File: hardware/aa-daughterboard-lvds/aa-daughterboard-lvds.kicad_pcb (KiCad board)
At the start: 4 copper layers, 148 parts, among them CN1 Barrel_Jack, CN10 6P6C, CN11 6P6C, CN12 6P6C, CN13 6P6C, CN14 Conn_01x08, CN15 Conn_01x08, CN16 Conn_01x08, CN17 8P8C, CN18 8P8C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

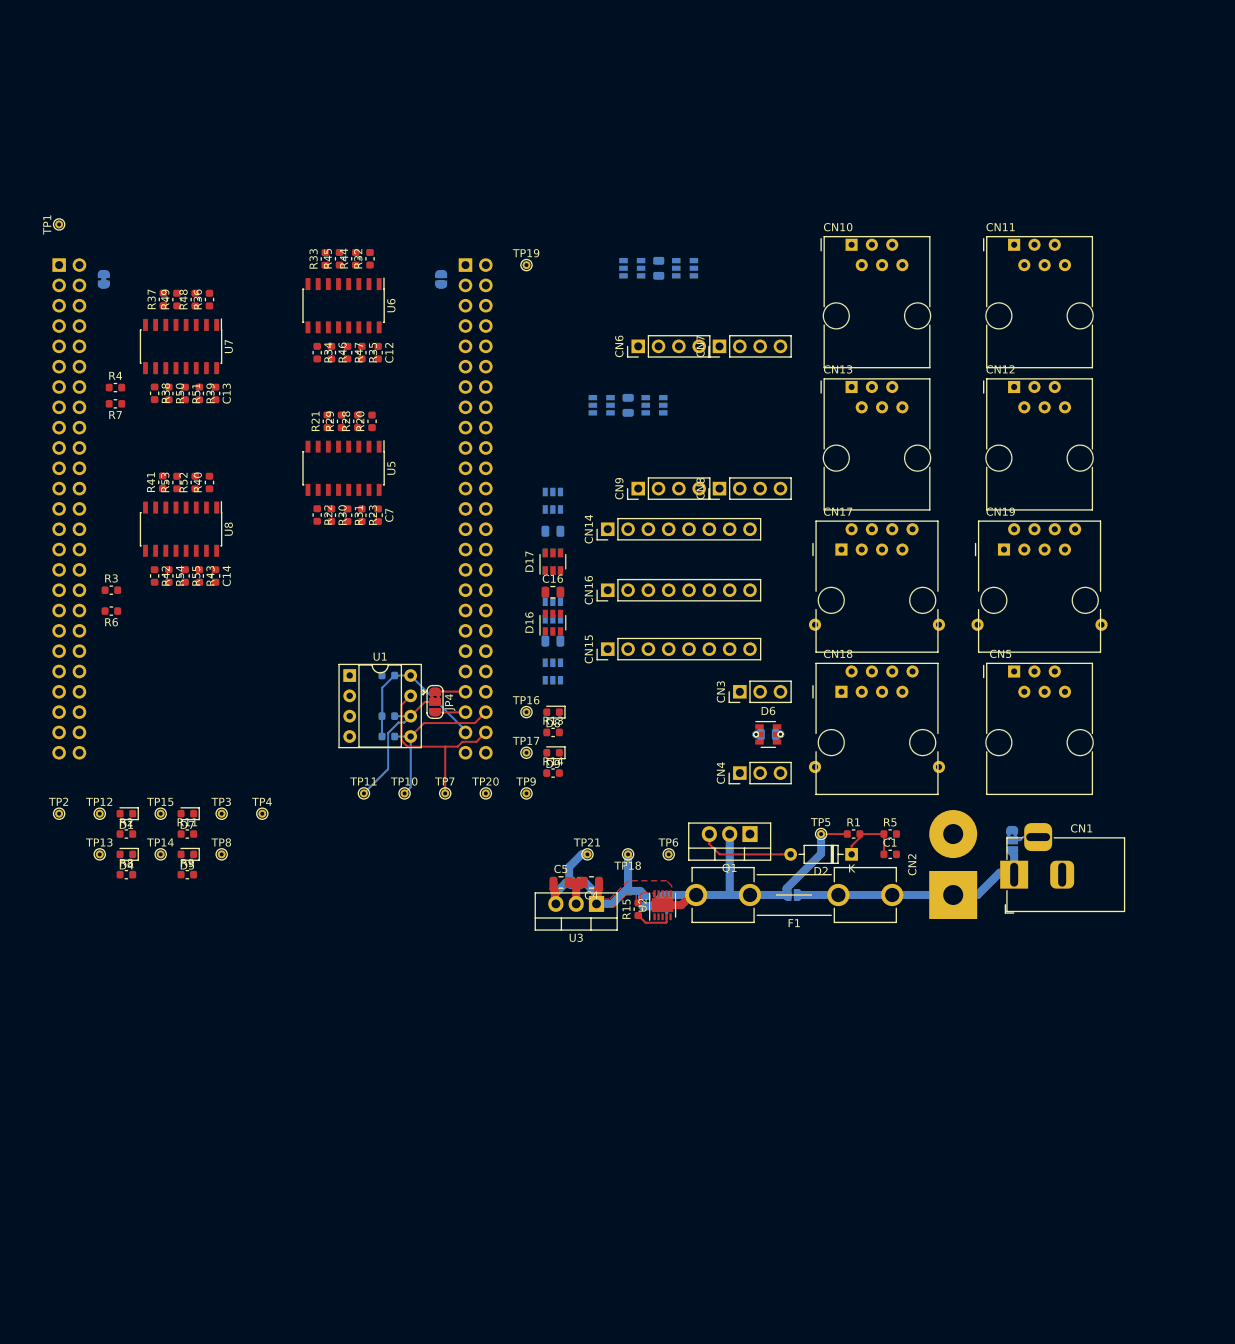
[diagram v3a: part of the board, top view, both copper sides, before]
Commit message: Name differential pairs, convert inconvenient 1x8 connectors to 2x4
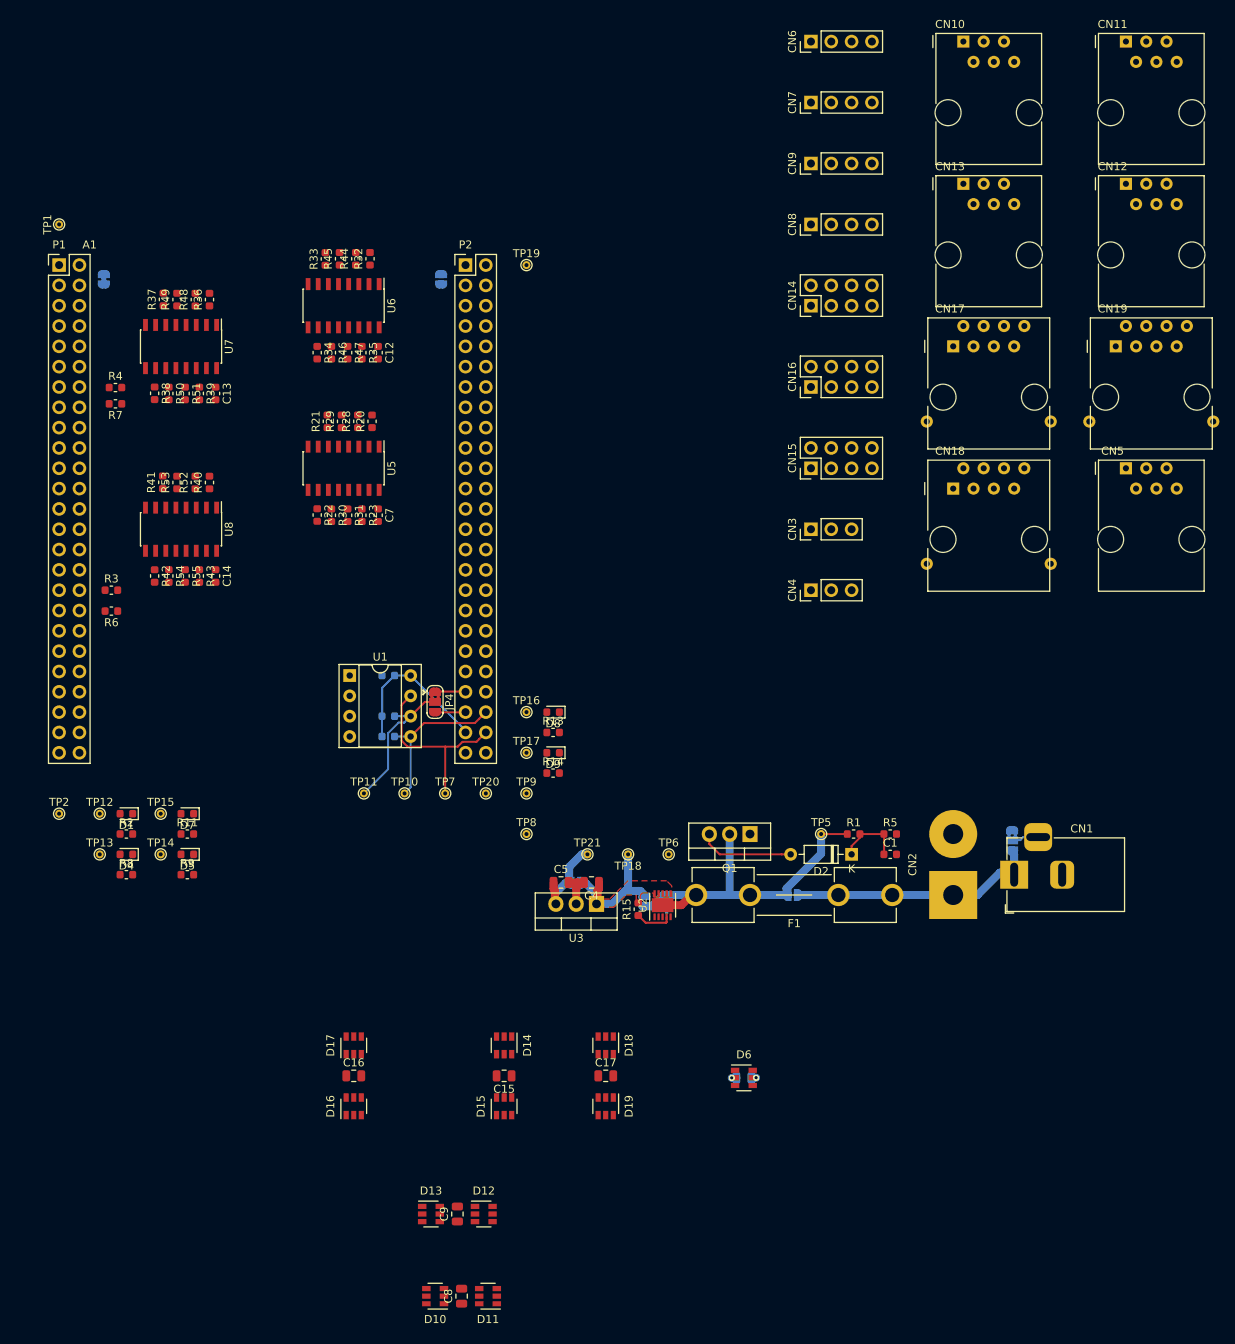
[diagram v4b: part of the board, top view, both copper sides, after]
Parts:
- removed P1, P2: Conn_02x25_Odd_Even, Connector_PinSocket_2.54mm:PinSocket_2x25_P2.54mm_Vertical
- removed TP3, TP4: TestPoint, TestPoint:TestPoint_THTPad_D1.0mm_Drill0.5mm
- added A1: STM32F407_Discovery_P1_P2, aa-daughterboard-lvds:STM32F407_Discovery_P1_P2_Socket, F.Cu at (45.7, 61.0)
- C15, C17, C8, C9, D10, D11, D12, D13, D14, D15, D18, D19: moved to F.Cu
- CN14, CN15, CN16: footprint Connector_PinHeader_2.54mm:PinHeader_1x08_P2.54mm_Vertical -> Connector_PinHeader_2.54mm:PinHeader_2x04_P2.54mm_Vertical
- moved C8 130.8 mm to (96.0, 189.8), turned to 90 degrees
- moved D10 130.8 mm to (92.7, 189.8)
- moved D11 130.8 mm to (99.3, 189.8)
- moved C9 103.3 mm to (95.5, 179.6), turned to 90 degrees
- moved D12 103.3 mm to (98.8, 179.6)
- moved D13 103.3 mm to (92.2, 179.6)
- moved D15 75.9 mm to (101.3, 166.1), turned to 90 degrees
- moved C15 68.3 mm to (101.3, 162.3)
- moved C16 65.4 mm to (82.5, 162.3)
- moved D16 65.4 mm to (82.5, 166.1)
- moved D17 65.4 mm to (82.5, 158.5)
- moved D19 62.3 mm to (114.0, 166.1), turned to 270 degrees
- moved D14 60.8 mm to (101.3, 158.5), turned to 270 degrees
- moved C17 54.8 mm to (114.0, 162.3)
- moved D18 47.2 mm to (114.0, 158.5), turned to 270 degrees
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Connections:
- net Net-(CN10-Pad2) renamed /PWM_CAP_1_P
- net Net-(CN10-Pad3) renamed /TX_STALK_1_P
- net Net-(CN10-Pad4) renamed /TX_STALK_1_N
- net Net-(CN10-Pad5) renamed /PWM_CAP_1_N
- net Net-(CN11-Pad2) renamed /PWM_CAP_B_P
- net Net-(CN11-Pad3) renamed /TX_STALK_B_P
- net Net-(CN11-Pad4) renamed /TX_STALK_B_N
- net Net-(CN11-Pad5) renamed /PWM_CAP_B_N
- net Net-(CN12-Pad2) renamed /PWM_CAP_2_P
- net Net-(CN12-Pad3) renamed /TX_STALK_2_P
- net Net-(CN12-Pad4) renamed /TX_STALK_2_N
- net Net-(CN12-Pad5) renamed /PWM_CAP_2_N
- net Net-(CN13-Pad2) renamed /PWM_CAP_A_P
- net Net-(CN13-Pad3) renamed /TX_STALK_A_P
- net Net-(CN13-Pad4) renamed /TX_STALK_A_N
- net Net-(CN13-Pad5) renamed /PWM_CAP_A_N
- net Net-(CN14-Pad1) renamed /TX_PANEL_0_P
- net Net-(CN14-Pad2) renamed /TX_PANEL_0_N
- net Net-(CN14-Pad3) renamed /TX_PANEL_1_P
- net Net-(CN14-Pad4) renamed /TX_PANEL_1_N
- net Net-(CN14-Pad5) renamed /TX_PANEL_2_P
- net Net-(CN14-Pad6) renamed /TX_PANEL_2_N
- net Net-(CN14-Pad7) renamed /TX_PANEL_3_P
- net Net-(CN14-Pad8) renamed /TX_PANEL_3_N
- net Net-(CN15-Pad1) renamed /TX_PANEL_4_P
- net Net-(CN15-Pad2) renamed /TX_PANEL_4_N
- net Net-(CN15-Pad3) renamed /TX_PANEL_5_P
- net Net-(CN15-Pad4) renamed /TX_PANEL_5_N
- net Net-(CN15-Pad5) renamed /TX_PANEL_6_P
- net Net-(CN15-Pad6) renamed /TX_PANEL_6_N
- net Net-(CN15-Pad7) renamed /TX_PANEL_7_P
- net Net-(CN15-Pad8) renamed /TX_PANEL_7_N
- net Net-(CN16-Pad1) renamed /TX_XP_0_P
- net Net-(CN16-Pad2) renamed /TX_XP_0_N
- net Net-(CN16-Pad3) renamed /TX_XP_1_P
- net Net-(CN16-Pad4) renamed /TX_XP_1_N
- net Net-(CN16-Pad5) renamed /TX_XP_2_P
- net Net-(CN16-Pad6) renamed /TX_XP_2_N
- net Net-(CN16-Pad7) renamed /TX_XP_3_P
- net Net-(CN16-Pad8) renamed /TX_XP_3_N
- net Net-(CN3-Pad1) renamed /TX_INPUT_S
- net Net-(CN3-Pad2) renamed /RX_INPUT_S
- net Net-(CN4-Pad1) renamed /TX_DEBUG_S
- net Net-(CN4-Pad2) renamed /RX_DEBUG_S
- JP4 pad 1: /PA8 -> Net-(A1-PadP2_43)
- JP4 pad 3: /PC8 -> Net-(A1-PadP2_45)
- R3 pad 1: /PB10 -> /TX_INPUT
- R4 pad 1: /PA2 -> /TX_DEBUG
- R6 pad 2: /PB11 -> /RX_INPUT
- R7 pad 2: /PA3 -> /RX_DEBUG
- U4 pad 1: /PE0 -> /TX_STALK_1
- U4 pad 15: /PB15 -> /PWM_CAP_B
- U4 pad 7: /PB13 -> /PWM_CAP_1
- U4 pad 9: /PE1 -> /TX_STALK_B
- U5 pad 1: /PE3 -> /TX_STALK_2
- U5 pad 15: /PB8 -> /PWM_CAP_A
- U5 pad 7: /PB9 -> /PWM_CAP_2
- U5 pad 9: /PE2 -> /TX_STALK_A
- U6 pad 1: /PE4 -> /TX_PANEL_0
- U6 pad 15: /PE7 -> /TX_PANEL_3
- U6 pad 7: /PE5 -> /TX_PANEL_1
- U6 pad 9: /PE6 -> /TX_PANEL_2
- U7 pad 1: /PE8 -> /TX_PANEL_4
- U7 pad 15: /PE11 -> /TX_PANEL_7
- U7 pad 7: /PE9 -> /TX_PANEL_5
- U7 pad 9: /PE10 -> /TX_PANEL_6
- U8 pad 1: /PE12 -> /TX_XP_0
- U8 pad 15: /PE15 -> /TX_XP_3
- U8 pad 7: /PE13 -> /TX_XP_1
- U8 pad 9: /PE14 -> /TX_XP_2
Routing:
- net Net-(A1-PadP2_43): track 0.00 -> 3.82 mm
- net /PA8: track 3.82 -> 0.00 mm
- net Net-(A1-PadP2_45): track 0.00 -> 3.78 mm
- net /PC8: track 3.78 -> 0.00 mm
